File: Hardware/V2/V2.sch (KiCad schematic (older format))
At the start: 25 parts

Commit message: Acelerómetro añadido
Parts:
- removed C?: C_Small, symbol device:C_Small
- removed D? (x7): WS2812B, LED_SMD:LED_WS2812B_PLCC4_5.0x5.0mm_P3.2mm, symbol LED:WS2812B
- removed D?: LED_RGB, symbol device:LED_RGB
- removed RV?: R_POT, symbol device:R_POT
- removed S?: JOYSTICK_MINI, JOYSTICK_MINI, symbol SparkFun-Switches:JOYSTICK_MINI
- removed SW?: SW_Push_Dual, symbol Switch:SW_Push_Dual
- added C? (x7): 100n, symbol device:C_Small
- added D? (x7): WS2812B, LED_SMD:LED_WS2812B_PLCC4_5.0x5.0mm_P3.2mm, symbol LED:WS2812B
- added R? (x3): 220R, symbol device:R_Small
- added R? (x2): 22R, symbol device:R_Small
- added R?: 100k, symbol device:R_Small
- added R? (x3): 10K, symbol device:R_Small
- added RV?: 10k, symbol device:R_POT
- added S?: JOYSTICK_THUMB, JOYSTICK, symbol SparkFun-Switches:JOYSTICK_THUMB
- added SW? (x2): SW_Push_Dual, symbol Switch:SW_Push_Dual
- added U?: LIS3DH, LGA-16-3X3, symbol SparkFun-Sensors:LIS3DH
- D?: value LED_Small -> LED_G
- D?: value LED_Small -> LED_R
- D?: value LED_Small -> LED_Y
- D?: value LED_Small -> LED_B
- J?: value Conn_01x04_Female -> I2C_OLED
- R?: value R_Small -> 220R
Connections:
- net labels added: BTN1, BTN2, D+, D-, JOY-BTN, JOY-H, JOY-V, LDR, LED_B, LED_G, LED_R, LED_Y, NEO, POT, SCL, SDA, VUSB
- wire segments 0 -> 119
- no-connect marks 0 -> 2
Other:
- moved on the sheet: BZ?, D?, J?, R?, SW?, U?, Y?

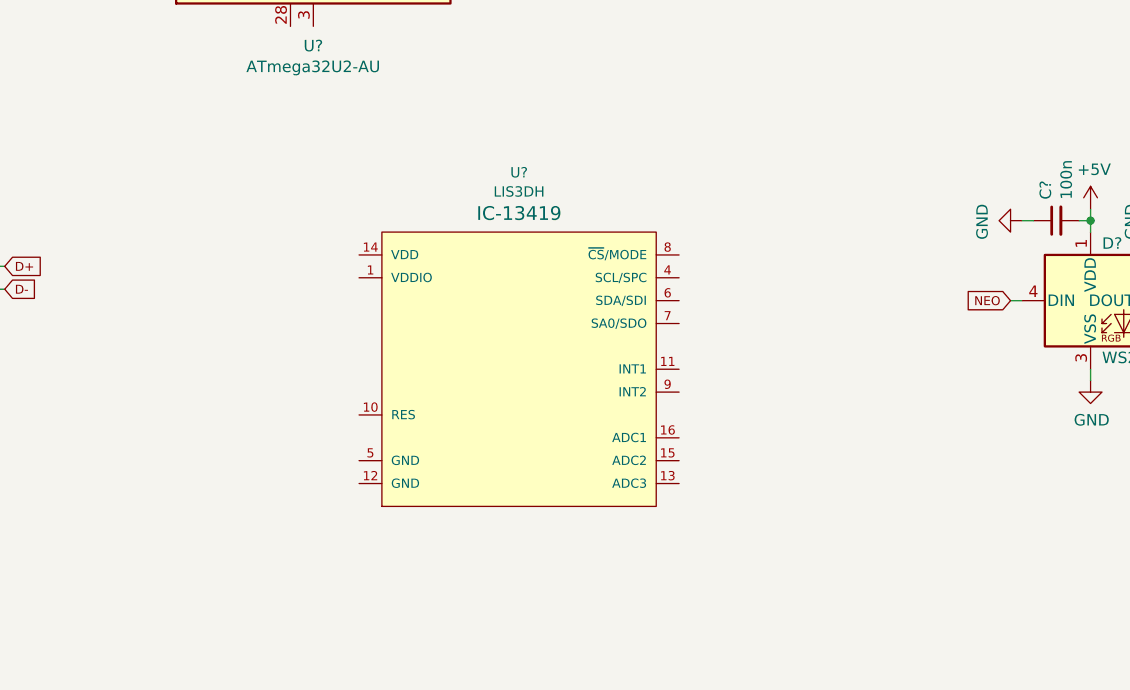
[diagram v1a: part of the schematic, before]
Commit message: Acelerómetro añadido
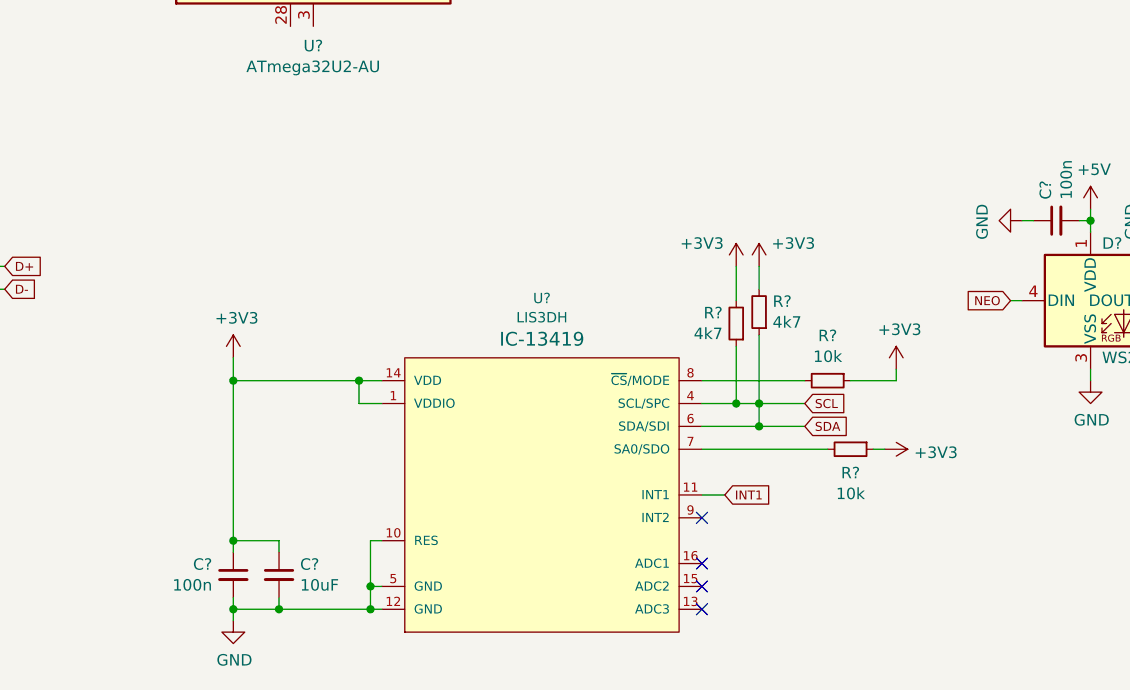
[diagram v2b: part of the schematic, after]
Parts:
- added C?: 10uF, symbol device:C_Small
- added C?: 100n, symbol device:C_Small
- added R? (x2): 10k, symbol device:R_Small
- added R? (x2): 4k7, symbol device:R_Small
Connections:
- net SDA is gone; now on net SCL: J?.4 (Pin_4)
- net GND: now also U?.10 (RES), U?.12 (GND), U?.5 (GND), C?.2, C?.2
- net SCL: now also U?.4 (SCL/SPC), U?.6 (SDA/SDI), R?.1, R?.1
- net +3V3: now reaches U?.1 (VDDIO)
- net +3V3: now also U?.14 (VDD), C?.1, C?.1, R?.1, R?.1, R?.2, R?.2
- net INT1: now reaches U?.11 (INT1)
- net at U?.7 (SA0/SDO): now also R?.2
- net at U?.8 (~CS~/MODE): now also R?.2
- no-connect marks 2 -> 6
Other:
- moved on the sheet: U?
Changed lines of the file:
@@
 L SparkFun-Sensors:LIS3DH U?
 U 1 1 5C90D393
-P 4150 6150
-F 0 "U?" H 4150 7010 45  0000 C CNN
-F 1 "LIS3DH" H 4150 6926 45  0000 C CNN
-F 2 "LGA-16-3X3" H 4150 6850 20  0001 C CNN
-F 3 "" H 4150 6150 60  0001 C CNN
-F 4 "IC-13419" H 4150 6831 60  0000 C CNN "Campo4"
-	1    4150 6150
-	1    0    0    -1
-$EndComp
+P 4250 6700
+F 0 "U?" H 4250 7560 45  0000 C CNN
+F 1 "LIS3DH" H 4250 7476 45  0000 C CNN
+F 2 "LGA-16-3X3" H 4250 7400 20  0001 C CNN
+F 3 "" H 4250 6700 60  0001 C CNN
+F 4 "IC-13419" H 4250 7381 60  0000 C CNN "Campo4"
+	1    4250 6700
+	1    0    0    -1
+$EndComp
+$Comp
+L device:C_Small C?
+U 1 1 5C81863B
+P 3100 7050
+F 0 "C?" H 3192 7096 50  0000 L CNN
+F 1 "10uF" H 3192 7005 50  0000 L CNN
+F 2 "" H 3100 7050 50  0001 C CNN
+F 3 "~" H 3100 7050 50  0001 C CNN
+	1    3100 7050
+	1    0    0    -1
+$EndComp
+$Comp
+L device:C_Small C?
+U 1 1 5C818DC8
+P 2900 7050
+F 0 "C?" H 2808 7096 50  0000 R CNN
+F 1 "100n" H 2808 7005 50  0000 R CNN
+F 2 "" H 2900 7050 50  0001 C CNN
+F 3 "~" H 2900 7050 50  0001 C CNN
+	1    2900 7050
+	1    0    0    -1
+$EndComp
+Wire Wire Line
+	3550 6900 3500 6900
+Wire Wire Line
+	3500 6900 3500 7100
+Wire Wire Line
+	3500 7200 3550 7200
+Wire Wire Line
+	3550 7100 3500 7100
+Connection ~ 3500 7100
+Wire Wire Line
+	3500 7100 3500 7200
+Wire Wire Line
+	3500 7200 3100 7200
+Wire Wire Line
+	3100 7200 3100 7150
+Connection ~ 3500 7200
+Wire Wire Line
+	3100 7200 2900 7200
+Wire Wire Line
+	2900 7200 2900 7150
+Connection ~ 3100 7200
+Wire Wire Line
+	2900 7200 2900 7250
+Connection ~ 2900 7200
+$Comp
+L power:GND #PWR?
+U 1 1 5C830EFA
+P 2900 7250
+F 0 "#PWR?" H 2900 7000 50  0001 C CNN
+F 1 "GND" H 2905 7077 50  0000 C CNN
+F 2 "" H 2900 7250 50  0001 C CNN
+F 3 "" H 2900 7250 50  0001 C CNN
+	1    2900 7250
+	1    0    0    -1
+$EndComp
+Wire Wire Line
+	3550 6200 3450 6200
+Wire Wire Line
+	2900 6200 2900 6900
+Wire Wire Line
+	3550 6300 3450 6300
+Wire Wire Line
+	3450 6300 3450 6200
+Connection ~ 3450 6200
+Wire Wire Line
+	3450 6200 2900 6200
+Wire Wire Line
+	3100 6950 3100 6900
+Wire Wire Line
+	3100 6900 2900 6900
+Connection ~ 2900 6900
+Wire Wire Line
+	2900 6900 2900 6950
+Wire Wire Line
+	2900 6200 2900 6100
+Connection ~ 2900 6200
+$Comp
+L power:+3V3 #PWR?
+U 1 1 5C8489F3
+P 2900 6100
+F 0 "#PWR?" H 2900 5950 50  0001 C CNN
+F 1 "+3V3" H 2915 6273 50  0000 C CNN
+F 2 "" H 2900 6100 50  0001 C CNN
+F 3 "" H 2900 6100 50  0001 C CNN
+	1    2900 6100
+	1    0    0    -1
+$EndComp
+NoConn ~ 4950 7000
+NoConn ~ 4950 7100
+NoConn ~ 4950 7200
+NoConn ~ 4950 6800
+Wire Wire Line
+	4950 6700 5050 6700
+Wire Wire Line
+	4950 6400 5200 6400
+Wire Wire Line
+	4950 6300 5100 6300
+Wire Wire Line
+	4950 6200 5400 6200
+$Comp
+L device:R_Small R?
+U 1 1 5C87F46C
+P 5500 6200
+F 0 "R?" V 5304 6200 50  0000 C CNN
+F 1 "10k" V 5395 6200 50  0000 C CNN
+F 2 "" H 5500 6200 50  0001 C CNN
+F 3 "~" H 5500 6200 50  0001 C CNN
+	1    5500 6200
+	0    1    1    0
+$EndComp
+$Comp
+L power:+3V3 #PWR?
+U 1 1 5C87F8DE
+P 5800 6150
+F 0 "#PWR?" H 5800 6000 50  0001 C CNN
+F 1 "+3V3" H 5815 6323 50  0000 C CNN
+F 2 "" H 5800 6150 50  0001 C CNN
+F 3 "" H 5800 6150 50  0001 C CNN
+	1    5800 6150
+	1    0    0    -1
+$EndComp
+Wire Wire Line
+	5600 6200 5800 6200
+Wire Wire Line
+	5800 6200 5800 6150
+Wire Wire Line
+	5100 6300 5100 6050
+Connection ~ 5100 6300
+Wire Wire Line
+	5200 6300 5200 6000
+$Comp
+L device:R_Small R?
+U 1 1 5C89387F
+P 5200 5900
+F 0 "R?" H 5141 5854 50  0000 R CNN
+F 1 "4k7" H 5141 5945 50  0000 R CNN
+F 2 "" H 5200 5900 50  0001 C CNN
+F 3 "~" H 5200 5900 50  0001 C CNN
+	1    5200 5900
+	-1   0    0    1
+$EndComp
+$Comp
+L device:R_Small R?
+U 1 1 5C893B11
+P 5100 5950
+F 0 "R?" H 5159 5904 50  0000 L CNN
+F 1 "4k7" H 5159 5995 50  0000 L CNN
+F 2 "" H 5100 5950 50  0001 C CNN
+F 3 "~" H 5100 5950 50  0001 C CNN
+	1    5100 5950
+	-1   0    0    1
+$EndComp
+$Comp
+L power:+3V3 #PWR?
+U 1 1 5C89455D
+P 5100 5700
+F 0 "#PWR?" H 5100 5550 50  0001 C CNN
+F 1 "+3V3" H 4950 5800 50  0000 C CNN
+F 2 "" H 5100 5700 50  0001 C CNN
+F 3 "" H 5100 5700 50  0001 C CNN
+	1    5100 5700
+	1    0    0    -1
+$EndComp
+$Comp
+L power:+3V3 #PWR?
+U 1 1 5C894852
+P 5200 5700
+F 0 "#PWR?" H 5200 5550 50  0001 C CNN
+F 1 "+3V3" H 5350 5800 50  0000 C CNN
+F 2 "" H 5200 5700 50  0001 C CNN
+F 3 "" H 5200 5700 50  0001 C CNN
+	1    5200 5700
+	1    0    0    -1
+$EndComp
+Wire Wire Line
+	5200 5700 5200 5800
+Wire Wire Line
+	5100 5700 5100 5850
+Text GLabel 5400 6300 2    39   Input ~ 0
+SCL
+Text GLabel 5400 6400 2    39   Input ~ 0
+SDA
+Wire Wire Line
+	5200 6400 5200 6300
+Connection ~ 5200 6400
+Wire Wire Line
+	5200 6400 5400 6400
+Wire Wire Line
+	5100 6300 5200 6300
+$Comp
+L power:+3V3 #PWR?
+U 1 1 5C8ABB53
+P 5750 6500
+F 0 "#PWR?" H 5750 6350 50  0001 C CNN
+F 1 "+3V3" V 5765 6628 50  0000 L CNN
+F 2 "" H 5750 6500 50  0001 C CNN
+F 3 "" H 5750 6500 50  0001 C CNN
+	1    5750 6500
+	0    1    1    0
+$EndComp
+$Comp
+L device:R_Small R?
+U 1 1 5C8ABEC8
+P 5600 6500
+F 0 "R?" V 5704 6500 50  0000 C CNN
+F 1 "10k" V 5795 6500 50  0000 C CNN
+F 2 "" H 5600 6500 50  0001 C CNN
+F 3 "~" H 5600 6500 50  0001 C CNN
+	1    5600 6500
+	0    1    1    0
+$EndComp
+Wire Wire Line
+	4950 6500 5500 6500
+Wire Wire Line
+	5700 6500 5750 6500
+Text GLabel 5050 6700 2    39   Input ~ 0
+INT1
+Connection ~ 5200 6300
+Wire Wire Line
+	5200 6300 5400 6300
 $EndSCHEMATC

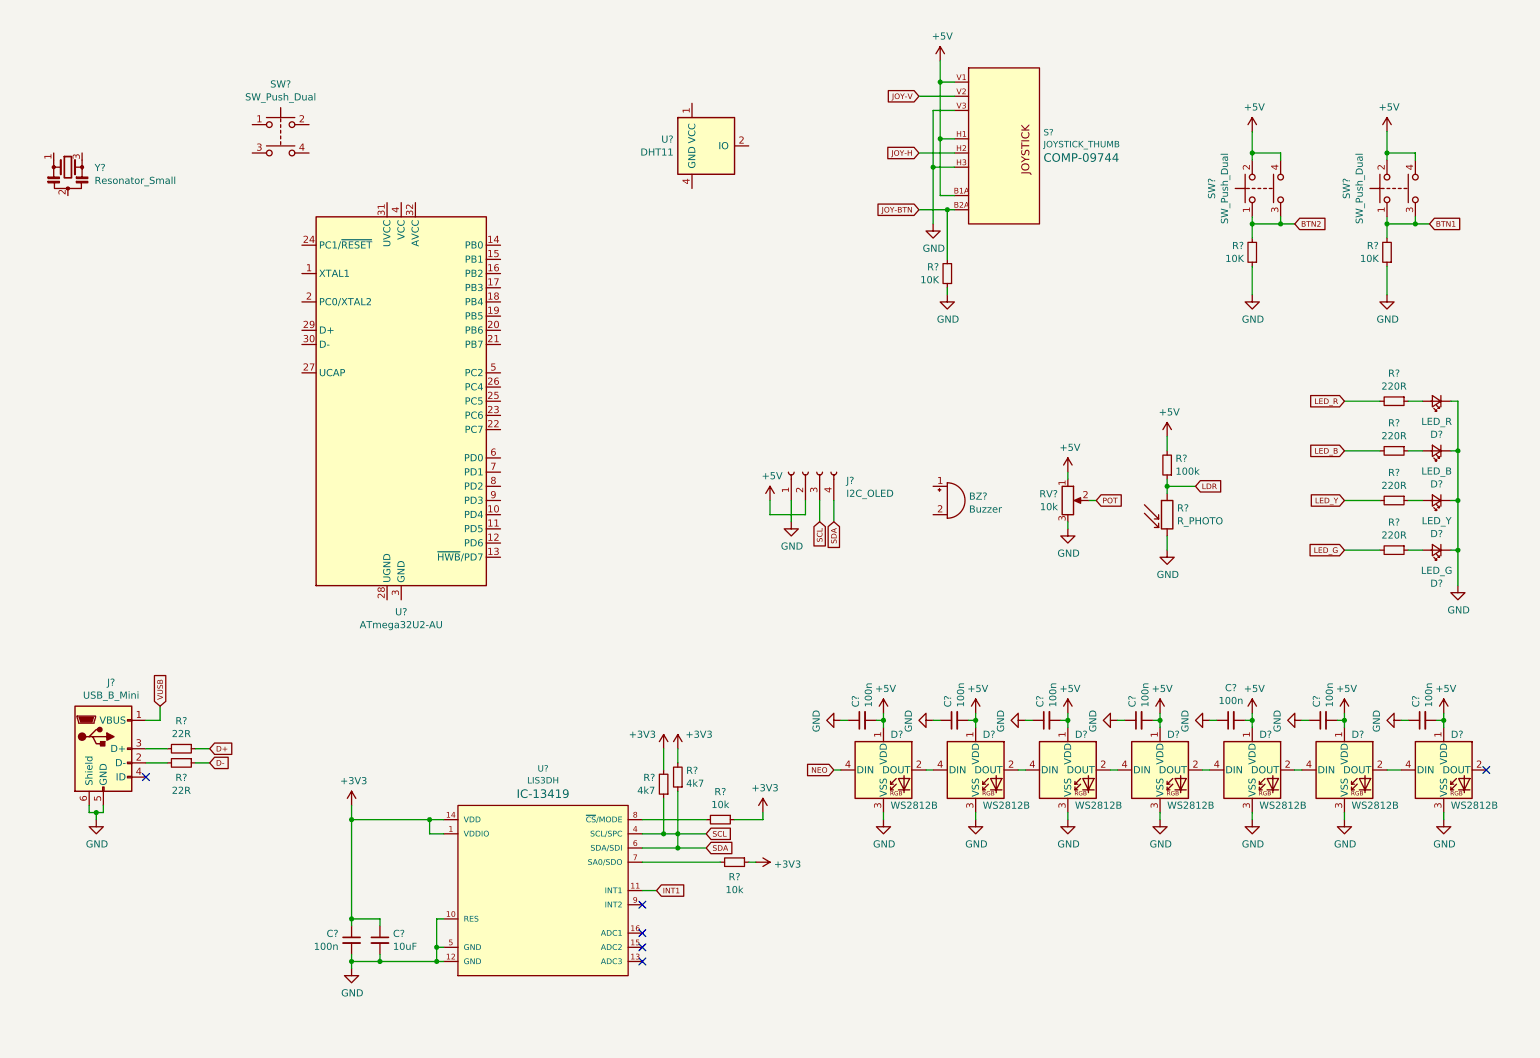
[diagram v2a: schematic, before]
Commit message: Cambiado a 3.3V
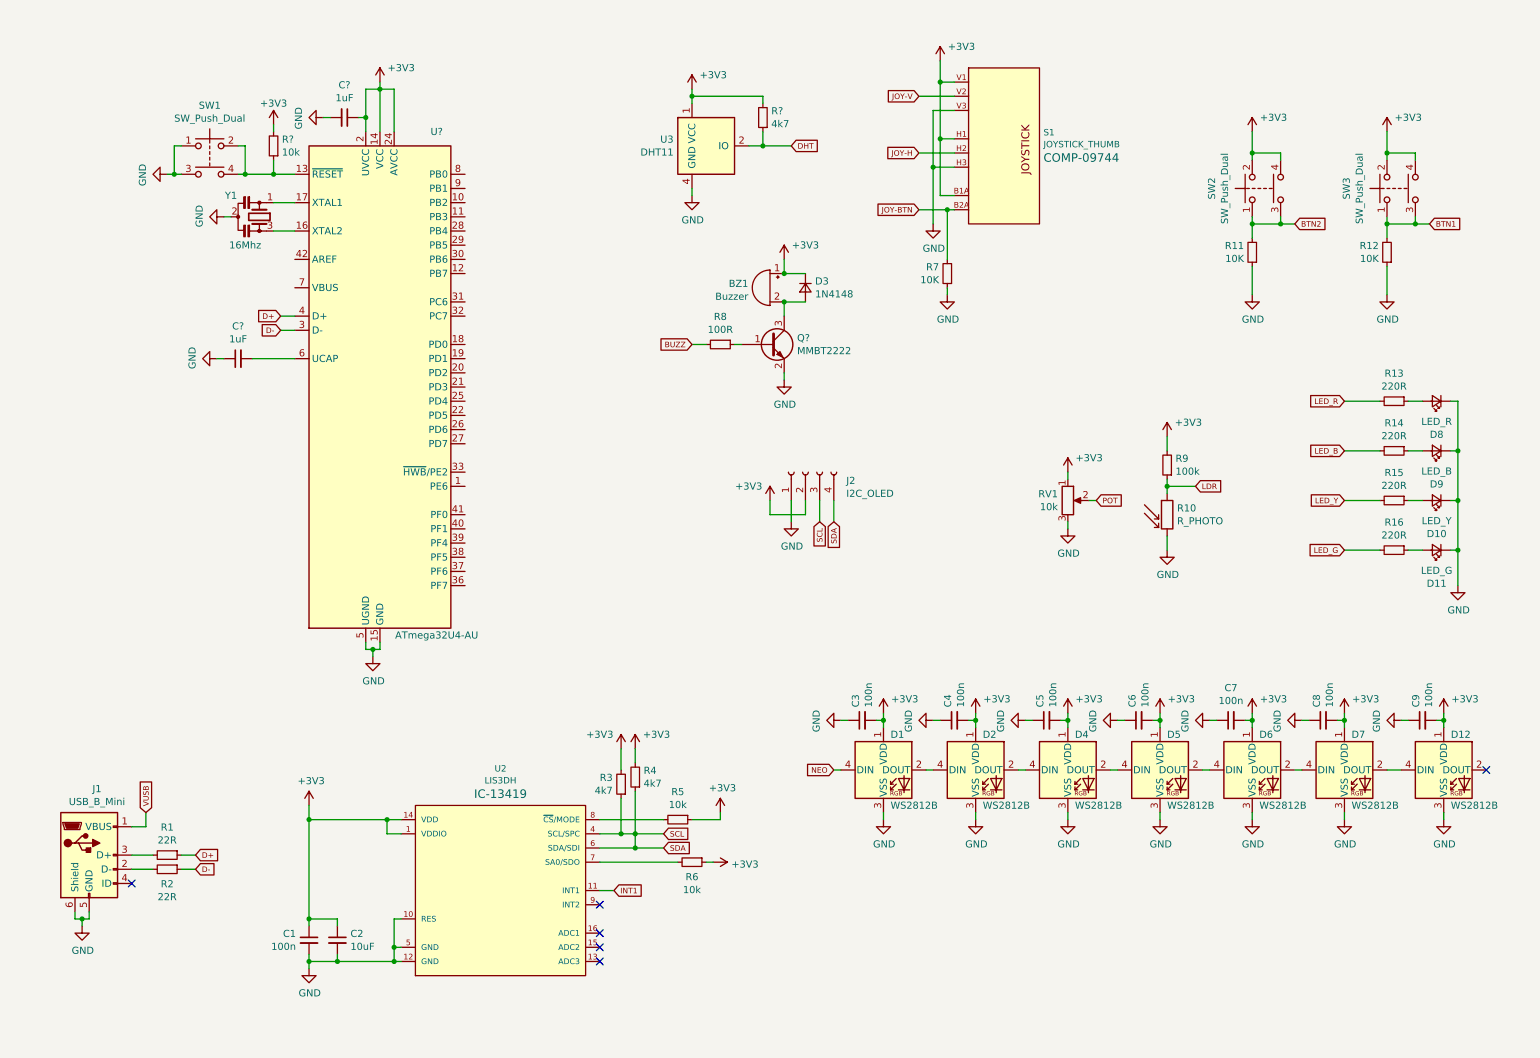
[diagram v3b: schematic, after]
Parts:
- removed U?: ATmega32U2-AU, Package_QFP:TQFP-32_7x7mm_P0.8mm, symbol MCU_Microchip_ATmega:ATmega32U2-AU
- added C? (x2): 1uF, symbol device:C_Small
- added D3: 1N4148, symbol device:D_Small
- added Q?: MMBT2222, symbol device:Q_NPN_BEC
- added R8: 100R, symbol device:R_Small
- added R?: 4k7, symbol device:R_Small
- added R?: 10k, symbol device:R_Small
- added U?: ATmega32U4-AU, Package_QFP:TQFP-44_10x10mm_P0.8mm, symbol MCU_Microchip_ATmega:ATmega32U4-AU
- Y1: renamed from Y?; value Resonator_Small -> 16Mhz
- gave numbers to parts that had none: 45
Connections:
- net +5V is gone; now on net +3V3: C3.2, C4.2, C5.2, C6.2, C7.2, C8.2, C9.2, D1.1 (VDD), D12.1 (VDD), D2.1 (VDD), D4.1 (VDD), D5.1 (VDD), D6.1 (VDD), D7.1 (VDD), J2.2 (Pin_2), R9.2, RV1.1, S1.B1A (SEL+), S1.H1 (H+), S1.V1 (V+), SW2.2, SW2.4, SW3.2, SW3.4
- net +3V3: now also BZ1.1 (-), U3.1 (VCC), C?.1, D3.1 (K), R?.2, R?.2, U?.14 (VCC), U?.2 (UVCC), U?.24 (AVCC), U?.34 (VCC), U?.44 (AVCC)
- net D+: now also U?.4 (D+)
- net D-: now also U?.3 (D-)
- net GND: now also SW1.1, SW1.3, U3.4 (GND), Y1.2, C?.1, C?.2, Q?.2 (E), U?.15 (GND), U?.23 (GND), U?.35 (GND), U?.43 (GND), U?.5 (UGND)
- net at Y1.1: now also U?.17 (XTAL1)
- net at Y1.3: now also U?.16 (XTAL2)
- net at BZ1.2 (+): now also D3.2 (A), Q?.3 (C)
- net DHT: now reaches U3.2 (IO)
- net DHT: now also R?.1
- net at SW1.2: now also SW1.4, R?.1, U?.13 (~RESET)
- new net: Q?.1 (B), R8.1
- new net: C?.2, U?.6 (UCAP)
- new net BUZZ: R8.2
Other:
- moved on the sheet: BZ1, C1, C2, J1, R1, R2, R3, R4, R5, R6, SW1, U2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

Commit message: Esquema terminado
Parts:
- added C10: 1uF, symbol device:C_Small
- added C13: 100nF, symbol device:C_Small
- added D?: GREEN, symbol device:LED_Small
- added D?: RED, symbol device:LED_Small
- added J?: ICSP, symbol Connector_Generic:Conn_02x03_Odd_Even
- added R? (x2): 330, symbol device:R_Small
- gave numbers to parts that had none: 6
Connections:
- net +3V3: now also D?.2 (A), D?.2 (A), J?.2 (Pin_2)
- net BTN1: now also U1.25 (PD4)
- net BTN2: now also U1.31 (PC6)
- net BUZZ: now also U1.28 (PB4)
- net DHT: now also U1.32 (PC7)
- net GND: now also U1.33 (~HWB~/PE2), C10.2, C13.2, J?.6 (Pin_6)
- net JOY-BTN: now also U1.40 (PF1)
- net JOY-H: now also U1.38 (PF5)
- net JOY-V: now also U1.39 (PF4)
- net LDR: now also U1.36 (PF7)
- net LED_B: now also U1.12 (PB7)
- net LED_G: now also U1.30 (PB6)
- net LED_R: now also U1.26 (PD6)
- net LED_Y: now also U1.29 (PB5)
- net NEO: now also U1.1 (PE6)
- net POT: now also U1.37 (PF6)
- net SCL: now also U1.18 (PD0), U1.19 (PD1)
- net RST: now reaches R17.1, SW1.2, SW1.4, U1.13 (~RESET)
- net RST: now also J?.5 (Pin_5)
- net MOSI: now reaches U1.10 (PB2)
- net MOSI: now also J?.4 (Pin_4)
- net MISO: now reaches U1.11 (PB3)
- net MISO: now also J?.1 (Pin_1)
- net RXI: now reaches U1.20 (PD2)
- net TXO: now reaches U1.21 (PD3)
- net at U1.22 (PD5): now also R?.2
- net at U1.42 (AREF): now also C13.1
- net at U1.7 (VBUS): now also C10.1
- net at U1.8 (PB0): now also R?.2
- net SCK: now reaches U1.9 (PB1)
- net SCK: now also J?.3 (Pin_3)
- new net: D?.1 (K), R?.1 (x2)
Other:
- note added: "A0"
- note added: "A1"
- note added: "A2"
- note added: "A3"
- note added: "A4"
- note added: "A5"
- note added: "D10"
- note added: "D11"
- note added: "D12"
- note added: "D13"
- note added: "D2"
- note added: "D3"
- note added: "D4"
- note added: "D5"
- note added: "D6"
- note added: "D7"
- note added: "D8"
- note added: "D9"

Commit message: Esquema Terminado
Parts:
- added C14: 10uF, symbol device:C_Small
- added C15, C16, C17: 1uF, symbol device:C_Small
- added U4: AP2112K-3.3, Package_TO_SOT_SMD:SOT-23-5, symbol Regulator_Linear:AP2112K-3.3
- SW2: value SW_Push_Dual -> B2
- SW3: value SW_Push_Dual -> B1
- gave numbers to parts that had none: 5
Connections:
- net +3V3: now also C16.1, C17.1, U4.5 (VOUT)
- net GND: now also C14.2, C15.2, C16.2, C17.2, U4.2 (GND)
- net VUSB: now also C14.1, C15.1, U4.1 (VIN), U4.3 (EN)
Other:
- note added: "ACCELEROMETER"
- note added: "BUTTONS"
- note added: "BUZZER"
- note added: "DHT11"
- note added: "JOYSTICK"
- note added: "LDR"
- note added: "LEDs"
- note added: "MICROCONTROLLER"
- note added: "NEOPIXEL LEDS"
- note added: "OLED DISPLAY"
- note added: "POWER SUPPLY"
- note added: "SLIDER"
- note added: "USB / ICSP"
- moved on the sheet: BZ1, C1, C10, C11, C12, C13, C2, C3, C4, C5, C6, C7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
